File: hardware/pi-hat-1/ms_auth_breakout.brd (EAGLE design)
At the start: 65.5 x 57.8 mm, 38 parts, among them IC1 ULN2003AD, J11 BUCK_MODULEHORIZONTAL, J9 POWER_JACKPTH_LOCK, Q1 DMN3023L, Q2 DMN3023L, Q3 DMN3023L, Q4 DMN3023L, Q5 DMN3023L, Q6 DMN3023L

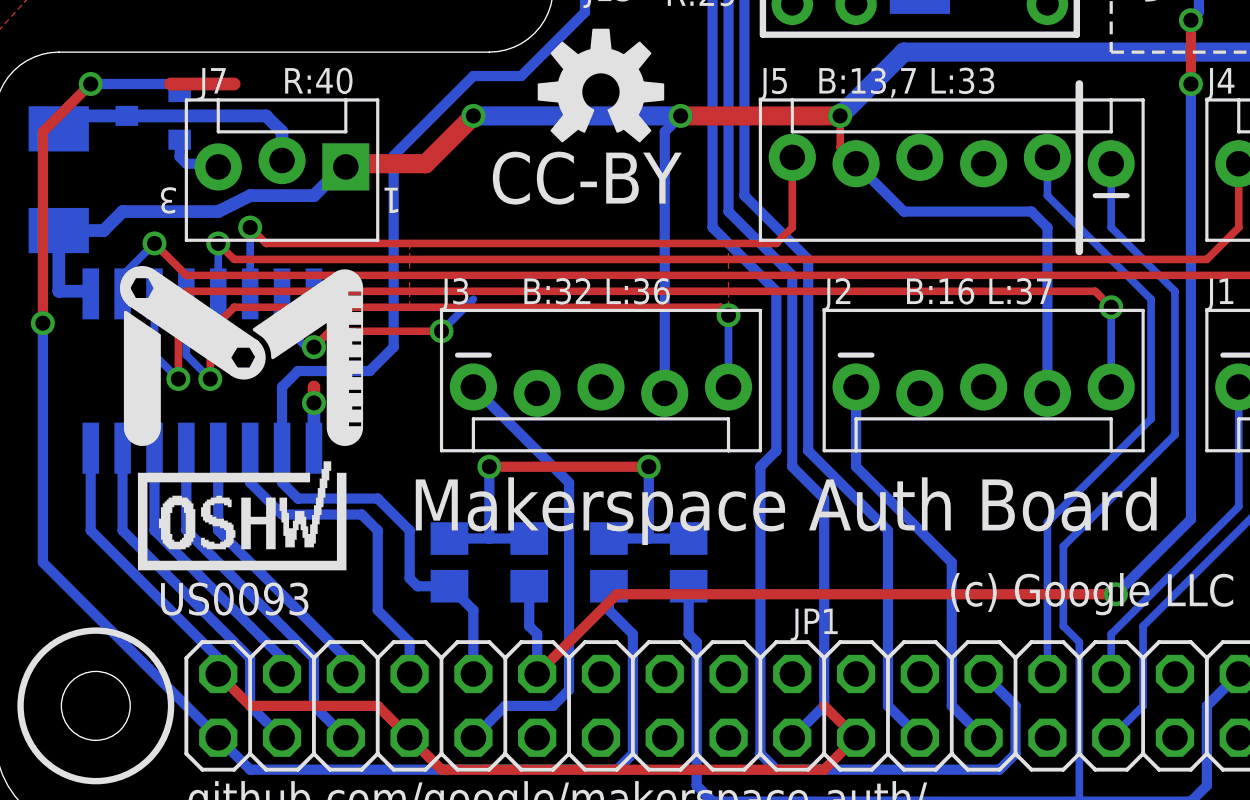
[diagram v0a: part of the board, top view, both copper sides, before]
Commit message: Rename JP1->J14, move some vias
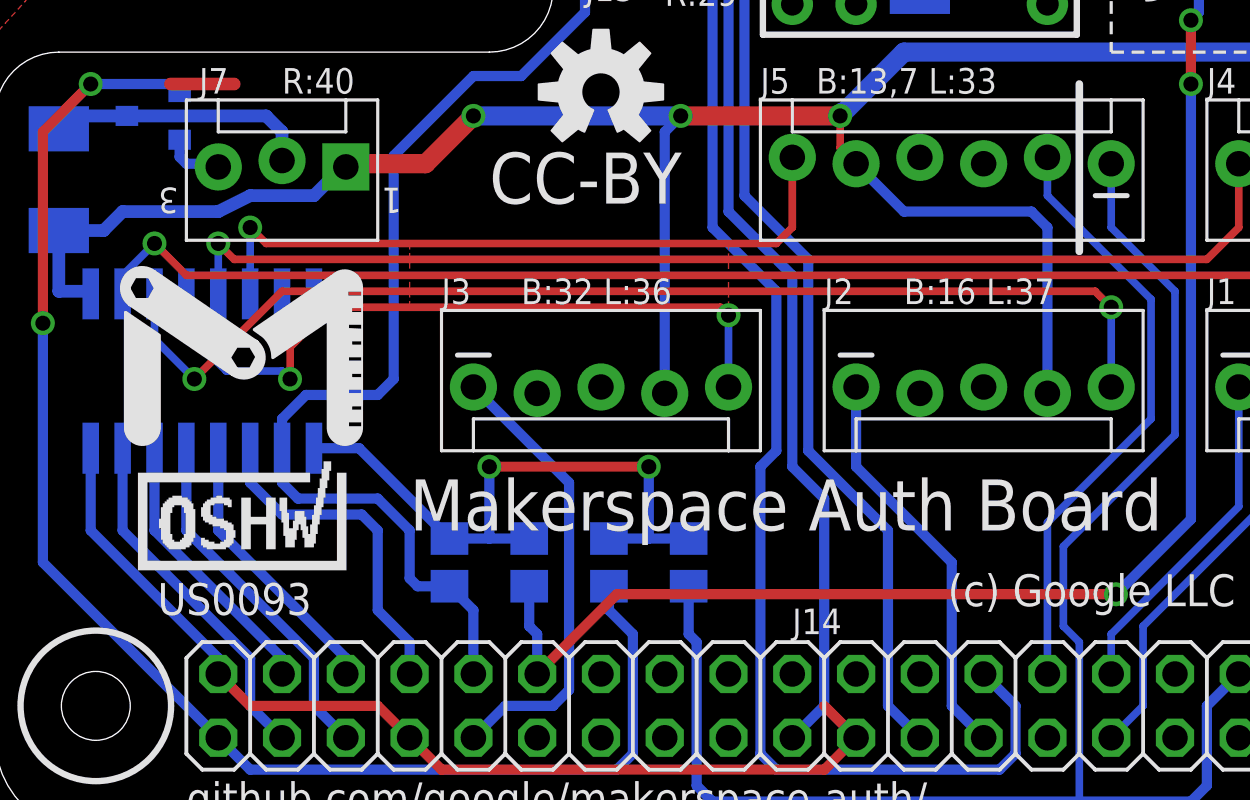
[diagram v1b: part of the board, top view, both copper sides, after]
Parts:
- renumbered JP1 to J14
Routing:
- net !L6: track 9.97 -> 0.00 mm, vias 2 -> 0
- net GND: track 94.0 -> 98.5 mm, vias 5 -> 4
- net !L2: track 47.7 -> 45.4 mm
- net !L3: track 29.7 -> 28.8 mm
